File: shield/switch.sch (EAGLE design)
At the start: 4 parts

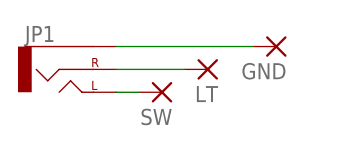
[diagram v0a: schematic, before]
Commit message: fix ground plane routing on switch mount board
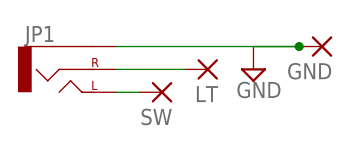
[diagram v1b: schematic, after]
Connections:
- net N$3 renamed GND
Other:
- moved on the sheet: GND
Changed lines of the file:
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@@
 </variantdefs>
 <classes>
-<class number="0" name="default" width="0" drill="0">
+<class number="0" name="default" width="0.3048" drill="0.508">
+<clearance class="0" value="0.254"/>
 </class>
 </classes>
@@
 <part name="LT" library="wirepad" deviceset="2,15/1,0" device=""/>
 <part name="GND" library="wirepad" deviceset="2,15/1,0" device=""/>
+<part name="SUPPLY1" library="supply2" deviceset="GND" device=""/>
 </parts>
 <sheets>
@@
 <instance part="SW" gate="1" x="66.04" y="38.1" rot="R180"/>
 <instance part="LT" gate="1" x="71.12" y="40.64" rot="R180"/>
-<instance part="GND" gate="1" x="78.74" y="43.18" rot="R180"/>
+<instance part="GND" gate="1" x="83.82" y="43.18" rot="R180"/>
+<instance part="SUPPLY1" gate="GND" x="76.2" y="40.64"/>
 </instances>
 <busses>
@@
 </segment>
 </net>
-<net name="N$3" class="0">
+<net name="GND" class="0">
 <segment>
 <pinref part="JP1" gate="G$1" pin="SLEEVE"/>
 <pinref part="GND" gate="1" pin="P"/>
-<wire x1="60.96" y1="43.18" x2="76.2" y2="43.18" width="0.1524" layer="91"/>
+<wire x1="60.96" y1="43.18" x2="81.28" y2="43.18" width="0.1524" layer="91"/>
+<pinref part="SUPPLY1" gate="GND" pin="GND"/>
+<junction x="81.28" y="43.18"/>
+<wire x1="81.28" y1="43.18" x2="76.2" y2="43.18" width="0.1524" layer="91"/>
 </segment>
 </net>
